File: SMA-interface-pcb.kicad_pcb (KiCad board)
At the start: 2 copper layers, 93 parts, among them J1 Conn_01x02_Pin, J10 Conn_01x04_Pin, J11 Conn_01x04_Pin, J12 USB_A_Stacked, J13 Conn_Coaxial, J14 Conn_Coaxial, J15 USB_A_Stacked, J2 Conn_01x02_Pin, J3 Conn_01x02_Pin, J4 Conn_Coaxial, J5 Conn_01x04_Pin, J6 Conn_01x04_Pin, J7 Conn_Coaxial, J8 Conn_Coaxial, J9 Conn_Coaxial, Q1 AO3400A, Q2 AO3400A, Q3 AO3400A, Q4 AO3400A, Q5 AO3400A, Q6 AO3400A, Q7 AO3400A, Q8 AO3400A, U1 74HC7014, U2 TMC2209_SILENTSTEPSTICK, U3 TMC2209_SILENTSTEPSTICK, U4 LM2596T-5, U5 TMC2209_SILENTSTEPSTICK, U6 TMC2209_SILENTSTEPSTICK

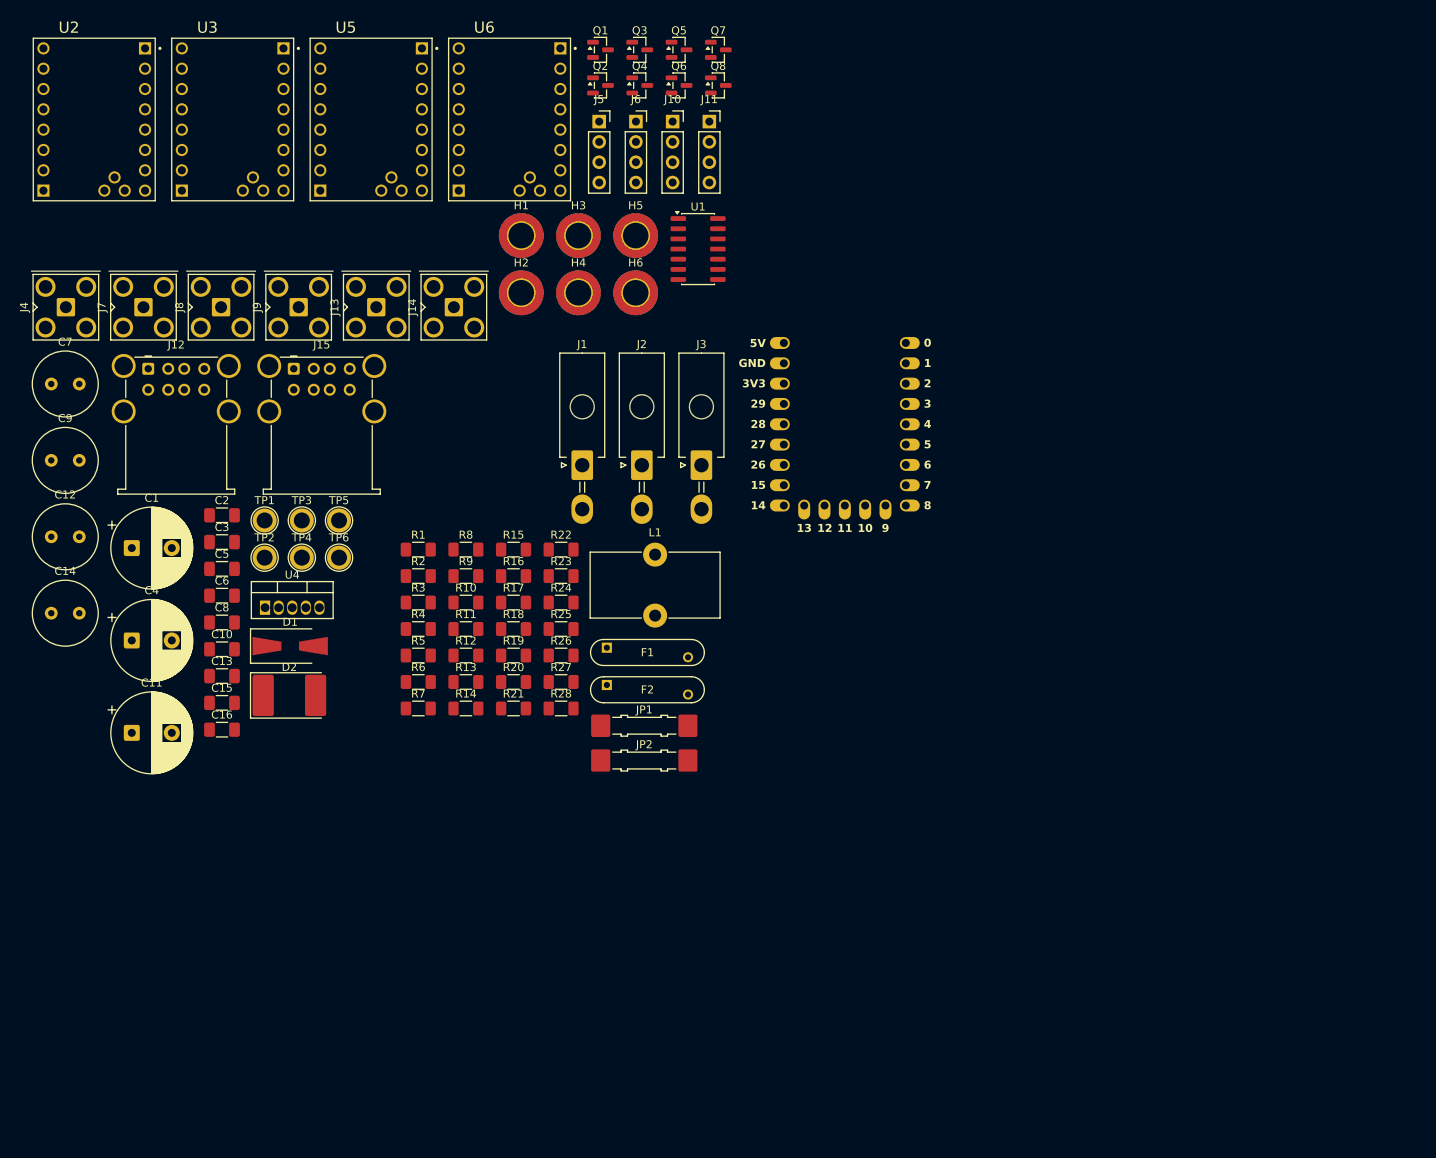
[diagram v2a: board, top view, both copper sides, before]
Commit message: first round of routing done
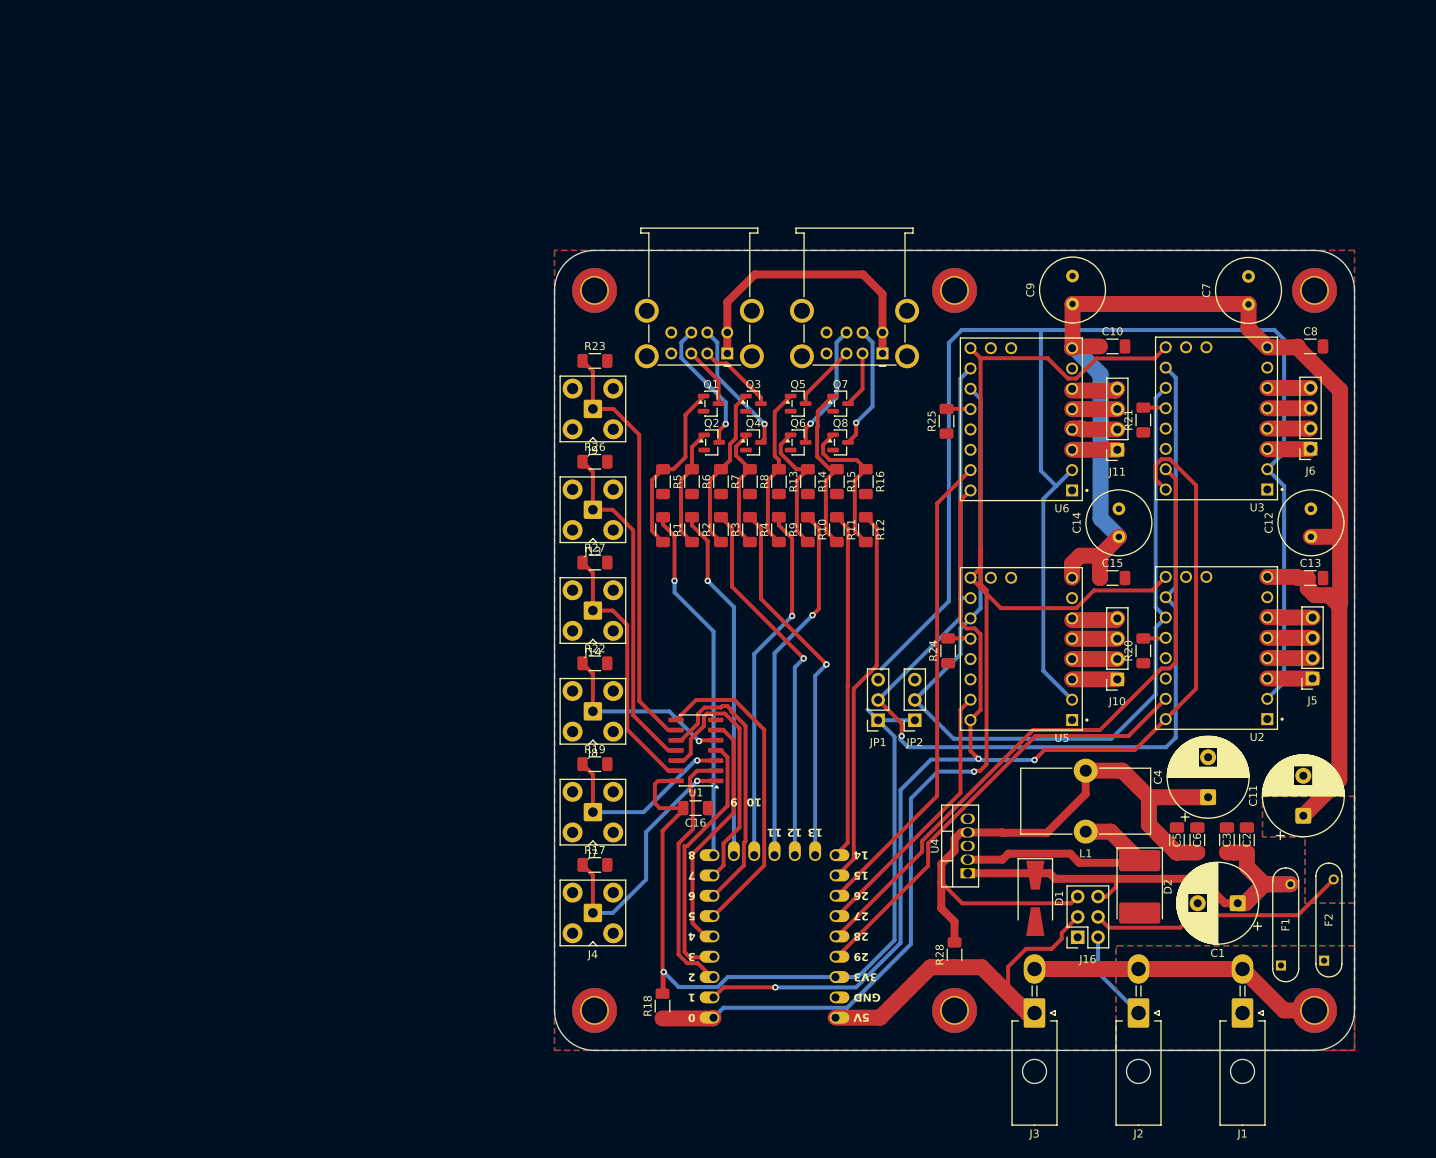
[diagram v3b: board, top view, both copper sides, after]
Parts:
- removed TP1, TP2, TP3, TP4, TP5, TP6: TestPoint, TestPoint:TestPoint_Plated_Hole_D2.0mm
- added J16: Conn_02x03_Odd_Even, Connector_PinSocket_2.54mm:PinSocket_2x03_P2.54mm_Vertical, F.Cu at (165.4, 135.8)
- J12, J15: footprint Connector_USB:USB_A_Wuerth_61400826021_Horizontal_Stacked -> NeuroACT:USB_A_Wuerth_61400826021_Horizontal_Stacked
- J13, J14, J4, J7, J8, J9: footprint Connector_Coaxial:SMA_Amphenol_901-143_Horizontal -> NeuroACT:SMA_Amphenol_901-143_Horizontal
- JP1, JP2: footprint Jumper:Jumper_Harwin_S1621_P10.9mm -> Connector_PinSocket_2.54mm:PinSocket_1x03_P2.54mm_Vertical
- R17, R19, R22, R23, R26, R27: value 10 kΩ -> 10k
- U2, U3, U5, U6: footprint NeuroACT:MODULE_TMC2208_SILENTSTEPSTICK -> NeuroACT:MODULE_TMC2209_SILENTSTEPSTICK
- moved C12 157.5 mm to (194.6, 85.8), turned to 90 degrees
- moved U2 155.1 mm to (182.8, 99.7), turned to 180 degrees
- moved C7 150.0 mm to (186.8, 56.7), turned to 90 degrees
- moved C11 146.8 mm to (193.6, 120.6), turned to 90 degrees
- moved C1 145.2 mm to (185.4, 131.6), turned to 180 degrees
- moved C8 140.4 mm to (194.5, 62.0)
- moved H1 138.6 mm to (195.0, 145.0)
- moved C13 136.6 mm to (194.5, 90.9)
- moved C4 136.0 mm to (181.7, 118.3), turned to 90 degrees
- moved C2 134.4 mm to (186.6, 123.7), turned to 90 degrees
- moved C14 133.8 mm to (170.6, 85.8), turned to 90 degrees
- moved C3 131.0 mm to (184.1, 123.7), turned to 90 degrees
- moved C9 129.1 mm to (164.8, 56.7), turned to 90 degrees
- moved U3 128.5 mm to (182.8, 71.0), turned to 180 degrees
- moved C6 125.7 mm to (180.3, 123.7), turned to 90 degrees
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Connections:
- H1 pad 1: (no net) -> GND
- H2 pad 1: (no net) -> GND
- H3 pad 1: (no net) -> GND
- H4 pad 1: (no net) -> GND
- H5 pad 1: (no net) -> GND
- H6 pad 1: (no net) -> GND
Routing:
- net /3.3V: track 0.00 -> 289.7 mm, vias 0 -> 1
- net /24V_motor: track 0.00 -> 189.5 mm
- net /Enable: track 0.00 -> 174.9 mm, vias 0 -> 1
- net /Direction: track 0.00 -> 160.0 mm, vias 0 -> 3
- net /MS1: track 0.00 -> 136.9 mm, vias 0 -> 1
- net /MS2: track 0.00 -> 117.1 mm
- net /5V_main: track 0.00 -> 82.2 mm
- net /mot_step_B: track 0.00 -> 82.2 mm
- net /+5V_BUCK: track 0.00 -> 82.1 mm
- net /24V_protected: track 0.00 -> 61.6 mm
- net /mot_step_D: track 0.00 -> 60.3 mm
- net /mot_step_A: track 0.00 -> 56.3 mm
- net Net-(J9-In): track 0.00 -> 53.1 mm
- net /Dout_sound_D: track 0.00 -> 47.6 mm
- net /Dout_sound_A: track 0.00 -> 47.0 mm, vias 0 -> 1
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- added copper zone on B.Cu, net /24V_input
- added copper zone on F.Cu, net /24V_input
- added copper zone on B.Cu, net /24V_motor
- added copper zone on F.Cu, net /24V_motor
- added copper zone on B.Cu, net GND
- added copper zone on F.Cu, net GND
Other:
- board outline added: 100 x 100 mm

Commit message: footprint placement V1
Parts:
- added G***: LOGO, NeuroACT:OSHW_logo, B.Cu at (127.5, 92.3)
- added G***: LOGO, NeuroACT:NeuroACT_logo, B.Cu at (127.5, 75.8)
- C12, C14, C7, C9: footprint Capacitor_THT:C_Radial_D8.0mm_H11.5mm_P3.50mm -> NeuroACT:CP_Radial_horizontal_D8.0mm_P3.50mm
- C4: footprint Capacitor_THT:CP_Radial_D10.0mm_P5.00mm -> Capacitor_THT:CP_Radial_D8.0mm_P5.00mm
- C5: value 1µF 16V -> 10µF 16V
- D1: value D_TVS -> SMBJ36CA
- D2: value SS56B -> SR5100; footprint Diode_SMD:D_3220_8050Metric_Pad2.65x5.15mm_HandSolder -> Diode_THT:D_DO-201AD_P15.24mm_Horizontal
- J1, J2, J3: footprint Connector_Molex:Molex_Mini-Fit_Jr_5569-02A2_2x01_P4.20mm_Horizontal -> NeuroACT:Molex_Mini-Fit_Jr_5569-02A2_2x01_P4.20mm_Horizontal
- J10, J11, J5, J6: footprint Connector_PinSocket_2.54mm:PinSocket_1x04_P2.54mm_Vertical -> Connector_PinHeader_2.54mm:PinHeader_1x04_P2.54mm_Vertical
- JP1, JP2: footprint Connector_PinSocket_2.54mm:PinSocket_1x03_P2.54mm_Vertical -> Connector_PinHeader_2.54mm:PinHeader_1x03_P2.54mm_Vertical
- R27: value 10k -> 0 ohm
- R28: value 0 ohm -> 10k
- U4: footprint Package_TO_SOT_THT:TO-220-5_Vertical -> NeuroACT:TO-220-5_Vertical
- moved R27 66.5 mm to (150.0, 138.0), turned to 90 degrees
- moved J4 63.0 mm to (104.8, 69.8)
- moved R17 62.7 mm to (106.5, 64.1)
- moved R25 46.1 mm to (179.8, 105.6), turned to 180 degrees
- moved R28 44.9 mm to (106.5, 127.1), turned to 0 degrees
- moved J5 38.7 mm to (169.5, 74.2)
- moved R23 38.1 mm to (106.5, 101.9)
- moved R26 38.1 mm to (106.5, 114.5)
- moved U2 38.0 mm to (158.5, 70.4)
- moved C12 37.9 mm to (157.1, 91.5), turned to 0 degrees
- moved J13 37.8 mm to (104.8, 120.2)
- moved J14 37.8 mm to (104.8, 132.8)
- moved J7 37.8 mm to (104.8, 82.4)
- moved J9 37.8 mm to (104.8, 107.6)
- moved R19 37.5 mm to (106.5, 76.7)
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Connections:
- J12 pad 9: GND -> (no net)
- J15 pad 9: GND -> (no net)
- R27 pad 1: Net-(J14-In) -> /5V_main
- R27 pad 2: GND -> /+5V_BUCK
- R28 pad 1: /5V_main -> Net-(J14-In)
- R28 pad 2: /+5V_BUCK -> GND
- RZ1 pad 17: /mot_step_D -> /mot_step_A
- RZ1 pad 18: /mot_step_C -> /mot_step_B
- RZ1 pad 19: /mot_step_B -> /mot_step_C
- RZ1 pad 20: /mot_step_A -> /mot_step_D
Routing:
- net /5V_main: track 82.2 -> 288.1 mm
- net /3.3V: track 289.7 -> 215.4 mm, vias 1 -> 0
- net /MS1: track 136.9 -> 89.2 mm
- net /24V_motor: track 189.5 -> 231.5 mm
- net Net-(J9-In): track 53.1 -> 25.5 mm
- net Net-(J4-In): track 32.2 -> 57.7 mm, vias 1 -> 0
- net Net-(J13-In): track 43.0 -> 18.4 mm
- net /Direction: track 160.0 -> 138.4 mm, vias 3 -> 1
- net /MS2: track 117.1 -> 97.8 mm, vias 0 -> 1
- net Net-(J7-In): track 24.6 -> 43.2 mm, vias 1 -> 0
- net /Dout_light_D: track 45.1 -> 62.7 mm, vias 1 -> 0
- net /Dout_light_C: track 44.9 -> 59.4 mm, vias 1 -> 0
- net /SMA_con4: track 39.5 -> 25.6 mm, vias 0 -> 1
- net /SMA_con6: track 32.7 -> 19.2 mm, vias 0 -> 1
- net /SMA_con5: track 35.2 -> 22.0 mm, vias 0 -> 1
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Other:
- board text added: "1"
- board text added: "2"
- board text added: "3"
- board text added: "4"
- board text added: "5"
- board text added: "6"
- board text added: "A"
- board text added: "B"
- board text added: "C"
- board text added: "D"
- board text added: "MS1"
- board text added: "MS2"
- board text added: "SMA Interface board v0.1, CERN-OHL-S-2.0"
